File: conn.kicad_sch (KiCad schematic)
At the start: 74 parts, among them J10 MicroFit_2x04, J11 JST_S4B-XH, J12 MicroFit_2x04, J13 JST_B2B-XH, J14 JST_S2B-XH, J15 DNI, J16 MLX_1x03, J17 MLX_1x03, J5 JST_S6B-XH, J6 JST_S4B-XH, J7 MicroFit_2x04, J8 JST_S4B-XH, J9 JST_S4B-XH, SW2 DNI

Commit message: Mostly groundplane declutter and loop removal.
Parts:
- renumbered D23 to D22, D22 to D23, NT26 to NT25, NT27 to NT26, NT25 to NT27, RN8 to RN7, RN7 to RN8
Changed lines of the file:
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@@
   (symbol (lib_id "power:GND") (at 147.32 58.42 0) (unit 1)
     (in_bom yes) (on_board yes)
-    (property "Reference" "#PWR046" (id 0) (at 147.32 64.77 0)
+    (property "Reference" "#PWR049" (id 0) (at 147.32 64.77 0)
       (effects (font (size 1.27 1.27)) hide)
     )
@@
   (symbol (lib_id "power:GND") (at 67.31 118.11 0) (unit 1)
     (in_bom yes) (on_board yes)
-    (property "Reference" "#PWR041" (id 0) (at 67.31 124.46 0)
+    (property "Reference" "#PWR042" (id 0) (at 67.31 124.46 0)
       (effects (font (size 1.27 1.27)) hide)
     )
@@
   (symbol (lib_id "3rd-party:NT_2_TT") (at 154.94 109.22 0) (unit 1)
     (in_bom yes) (on_board yes)
-    (property "Reference" "NT26" (id 0) (at 154.94 108.62 0)
+    (property "Reference" "NT25" (id 0) (at 154.94 108.62 0)
       (effects (font (size 0.6 0.6)))
     )
@@
   (symbol (lib_id "3rd-party:NT_2_TT") (at 167.64 80.01 90) (unit 1)
     (in_bom yes) (on_board yes)
-    (property "Reference" "NT25" (id 0) (at 167.04 80.01 0)
+    (property "Reference" "NT27" (id 0) (at 167.04 80.01 0)
       (effects (font (size 0.6 0.6)))
     )
@@
   (symbol (lib_id "power:GND") (at 87.63 58.42 0) (unit 1)
     (in_bom yes) (on_board yes)
-    (property "Reference" "#PWR042" (id 0) (at 87.63 64.77 0)
+    (property "Reference" "#PWR044" (id 0) (at 87.63 64.77 0)
       (effects (font (size 1.27 1.27)) hide)
     )
@@
   (symbol (lib_id "power:GND") (at 267.97 158.75 0) (unit 1)
     (in_bom yes) (on_board yes)
-    (property "Reference" "#PWR037" (id 0) (at 267.97 165.1 0)
+    (property "Reference" "#PWR058" (id 0) (at 267.97 165.1 0)
       (effects (font (size 1.27 1.27)) hide)
     )
@@
   (symbol (lib_id "power:+5V") (at 60.96 151.13 0) (unit 1)
     (in_bom yes) (on_board yes)
-    (property "Reference" "#PWR039" (id 0) (at 60.96 154.94 0)
+    (property "Reference" "#PWR040" (id 0) (at 60.96 154.94 0)
       (effects (font (size 1.27 1.27)) hide)
     )
@@
   (symbol (lib_id "Device:LED") (at 259.08 83.82 0) (unit 1)
     (in_bom yes) (on_board yes)
-    (property "Reference" "D22" (id 0) (at 255.27 80.01 0))
+    (property "Reference" "D23" (id 0) (at 255.27 80.01 0))
     (property "Value" "GRN" (id 1) (at 262.89 82.55 0))
     (property "Footprint" "-Project:LED_0402_DOT" (id 2) (at 259.08 83.82 0)
@@
   (symbol (lib_id "Device:R_Pack04") (at 236.22 85.09 270) (mirror x) (unit 1)
     (in_bom yes) (on_board yes)
-    (property "Reference" "RN8" (id 0) (at 233.68 93.98 90)
+    (property "Reference" "RN7" (id 0) (at 233.68 93.98 90)
       (effects (font (size 1.27 1.27)) (justify left))
     )
@@
   (symbol (lib_id "power:GND") (at 81.28 83.82 0) (unit 1)
     (in_bom yes) (on_board yes)
-    (property "Reference" "#PWR0103" (id 0) (at 81.28 90.17 0)
+    (property "Reference" "#PWR043" (id 0) (at 81.28 90.17 0)
       (effects (font (size 1.27 1.27)) hide)
     )
@@
   (symbol (lib_id "power:GND") (at 116.84 58.42 0) (unit 1)
     (in_bom yes) (on_board yes)
-    (property "Reference" "#PWR044" (id 0) (at 116.84 64.77 0)
+    (property "Reference" "#PWR047" (id 0) (at 116.84 64.77 0)
       (effects (font (size 1.27 1.27)) hide)
     )
@@
   (symbol (lib_id "power:GND") (at 187.96 73.66 0) (unit 1)
     (in_bom yes) (on_board yes)
-    (property "Reference" "#PWR051" (id 0) (at 187.96 80.01 0)
+    (property "Reference" "#PWR055" (id 0) (at 187.96 80.01 0)
       (effects (font (size 1.27 1.27)) hide)
     )
@@
   (symbol (lib_id "Device:R_Pack04") (at 236.22 134.62 270) (mirror x) (unit 1)
     (in_bom yes) (on_board yes)
-    (property "Reference" "RN7" (id 0) (at 233.68 143.51 90)
+    (property "Reference" "RN8" (id 0) (at 233.68 143.51 90)
       (effects (font (size 1.27 1.27)) (justify left))
     )
@@
   (symbol (lib_id "power:GND") (at 110.49 83.82 0) (unit 1)
     (in_bom yes) (on_board yes)
-    (property "Reference" "#PWR0102" (id 0) (at 110.49 90.17 0)
+    (property "Reference" "#PWR045" (id 0) (at 110.49 90.17 0)
       (effects (font (size 1.27 1.27)) hide)
     )
@@
   (symbol (lib_id "Device:LED") (at 259.08 78.74 180) (unit 1)
     (in_bom yes) (on_board yes)
-    (property "Reference" "D23" (id 0) (at 255.27 82.55 0))
+    (property "Reference" "D22" (id 0) (at 255.27 82.55 0))
     (property "Value" "RED" (id 1) (at 262.89 80.01 0))
     (property "Footprint" "-Project:LED_0402_DOT" (id 2) (at 259.08 78.74 0)
@@
   (symbol (lib_id "power:GND") (at 60.96 178.435 0) (unit 1)
     (in_bom yes) (on_board yes)
-    (property "Reference" "#PWR040" (id 0) (at 60.96 184.785 0)
+    (property "Reference" "#PWR041" (id 0) (at 60.96 184.785 0)
       (effects (font (size 1.27 1.27)) hide)
     )
@@
   (symbol (lib_id "power:+5V") (at 116.84 33.02 0) (unit 1)
     (in_bom yes) (on_board yes)
-    (property "Reference" "#PWR043" (id 0) (at 116.84 36.83 0)
+    (property "Reference" "#PWR046" (id 0) (at 116.84 36.83 0)
       (effects (font (size 1.27 1.27)) hide)
     )
@@
   (symbol (lib_id "power:GND") (at 165.1 130.175 0) (unit 1)
     (in_bom yes) (on_board yes)
-    (property "Reference" "#PWR047" (id 0) (at 165.1 136.525 0)
+    (property "Reference" "#PWR050" (id 0) (at 165.1 136.525 0)
       (effects (font (size 1.27 1.27)) hide)
     )
@@
   (symbol (lib_id "power:GND") (at 267.97 54.61 0) (unit 1)
     (in_bom yes) (on_board yes)
-    (property "Reference" "#PWR0105" (id 0) (at 267.97 60.96 0)
+    (property "Reference" "#PWR056" (id 0) (at 267.97 60.96 0)
       (effects (font (size 1.27 1.27)) hide)
     )
@@
   (symbol (lib_id "3rd-party:NT_2_TT") (at 154.94 111.76 0) (unit 1)
     (in_bom yes) (on_board yes)
-    (property "Reference" "NT27" (id 0) (at 154.94 111.16 0)
+    (property "Reference" "NT26" (id 0) (at 154.94 111.16 0)
       (effects (font (size 0.6 0.6)))
     )
@@
   (symbol (lib_id "power:GND") (at 267.97 106.68 0) (unit 1)
     (in_bom yes) (on_board yes)
-    (property "Reference" "#PWR053" (id 0) (at 267.97 113.03 0)
+    (property "Reference" "#PWR057" (id 0) (at 267.97 113.03 0)
       (effects (font (size 1.27 1.27)) hide)
     )
@@
   (symbol (lib_id "power:+5V") (at 167.64 77.47 0) (unit 1)
     (in_bom yes) (on_board yes)
-    (property "Reference" "#PWR045" (id 0) (at 167.64 81.28 0)
+    (property "Reference" "#PWR051" (id 0) (at 167.64 81.28 0)
       (effects (font (size 1.27 1.27)) hide)
     )
@@
   (symbol (lib_id "power:GND") (at 187.96 49.53 0) (unit 1)
     (in_bom yes) (on_board yes)
-    (property "Reference" "#PWR050" (id 0) (at 187.96 55.88 0)
+    (property "Reference" "#PWR054" (id 0) (at 187.96 55.88 0)
       (effects (font (size 1.27 1.27)) hide)
     )
@@
   (symbol (lib_id "power:GND") (at 140.97 85.09 0) (unit 1)
     (in_bom yes) (on_board yes)
-    (property "Reference" "#PWR0104" (id 0) (at 140.97 91.44 0)
+    (property "Reference" "#PWR048" (id 0) (at 140.97 91.44 0)
       (effects (font (size 1.27 1.27)) hide)
     )
@@
   (symbol (lib_id "power:+5V") (at 179.07 39.37 0) (unit 1)
     (in_bom yes) (on_board yes)
-    (property "Reference" "#PWR048" (id 0) (at 179.07 43.18 0)
+    (property "Reference" "#PWR052" (id 0) (at 179.07 43.18 0)
       (effects (font (size 1.27 1.27)) hide)
     )
@@
   (symbol (lib_id "power:+5V") (at 179.07 63.5 0) (unit 1)
     (in_bom yes) (on_board yes)
-    (property "Reference" "#PWR049" (id 0) (at 179.07 67.31 0)
-      (effects (font (size 1.27 1.27)) hide)
-    )
+    (property "Reference" "#PWR053" (id 0) (at 179.07 67.31 0)
+      (effects (font (size 1.27 1.27)) hide)
+    )

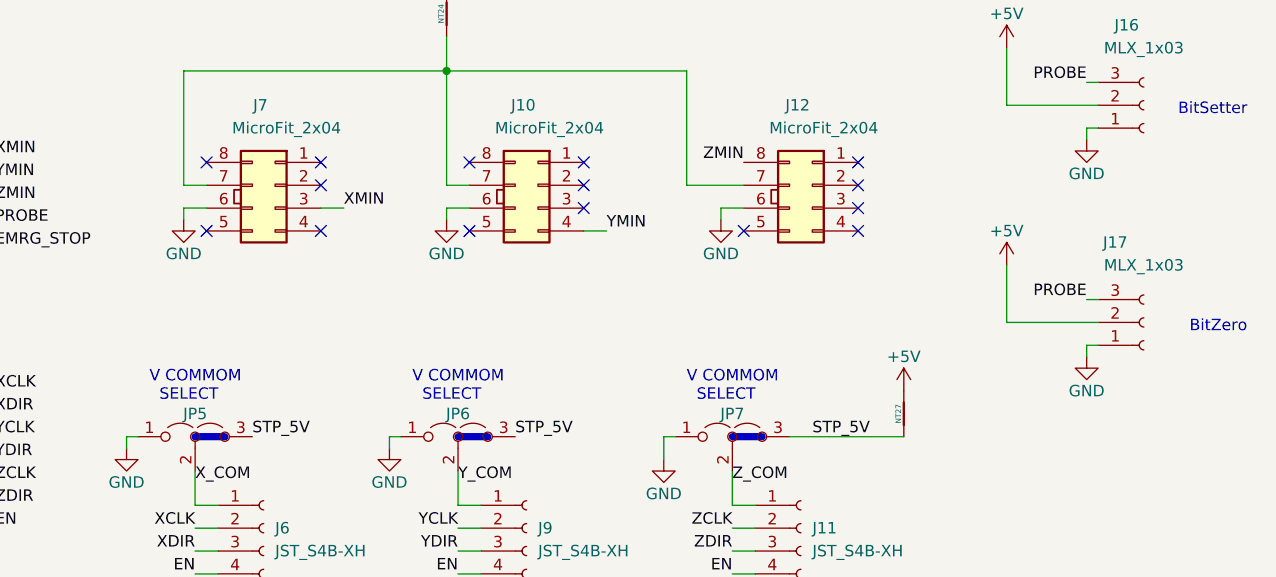
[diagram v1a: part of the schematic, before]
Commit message: Fixed opto-isolator wrong part and added jumper to isolate A/DGNDs.
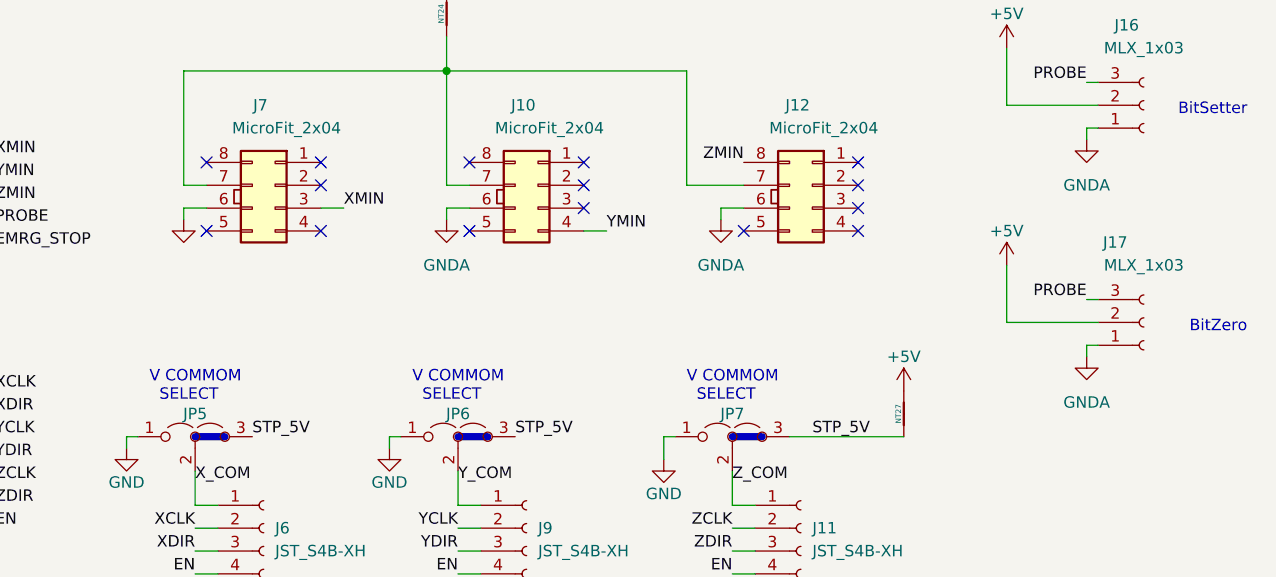
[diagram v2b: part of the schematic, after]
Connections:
- net GND: no longer J10.6 (Pin_6), J12.6 (Pin_6), J16.1 (Pin_1), J17.1 (Pin_1), J7.6 (Pin_6)
- new net GNDA: J10.6 (Pin_6), J12.6 (Pin_6), J16.1 (Pin_1), J17.1 (Pin_1), J7.6 (Pin_6)
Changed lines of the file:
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@@
     (pin "3")
-  )
-  (symbol (lib_id "power:GND") (at 147.32 58.42 0) (unit 1)
-    (in_bom yes) (on_board yes)
-    (property "Reference" "#PWR049" (id 0) (at 147.32 64.77 0)
-      (effects (font (size 1.27 1.27)) hide)
-    )
-    (property "Value" "GND" (id 1) (at 147.32 62.23 0))
-    (property "Footprint" "" (id 2) (at 147.32 58.42 0)
-      (effects (font (size 1.27 1.27)) hide)
-    )
-    (property "Datasheet" "" (id 3) (at 147.32 58.42 0)
-      (effects (font (size 1.27 1.27)) hide)
-    )
-    (pin "1")
   )
   (symbol (lib_id "Device:LED") (at 259.08 22.86 0) (unit 1)
@@
     (pin "2")
   )
+  (symbol (lib_id "power:GNDA") (at 147.32 58.42 0) (unit 1)
+    (in_bom yes) (on_board yes) (fields_autoplaced)
+    (property "Reference" "#PWR063" (id 0) (at 147.32 64.77 0)
+      (effects (font (size 1.27 1.27)) hide)
+    )
+    (property "Value" "GNDA" (id 1) (at 147.32 63.5 0))
+    (property "Footprint" "" (id 2) (at 147.32 58.42 0)
+      (effects (font (size 1.27 1.27)) hide)
+    )
+    (property "Datasheet" "" (id 3) (at 147.32 58.42 0)
+      (effects (font (size 1.27 1.27)) hide)
+    )
+    (pin "1")
+  )
   (symbol (lib_id "3rd-party:NT_2_TT") (at 50.8 170.18 0) (unit 1)
     (in_bom yes) (on_board yes)
@@
     (pin "1")
     (pin "2")
-  )
-  (symbol (lib_id "power:GND") (at 87.63 58.42 0) (unit 1)
-    (in_bom yes) (on_board yes)
-    (property "Reference" "#PWR044" (id 0) (at 87.63 64.77 0)
-      (effects (font (size 1.27 1.27)) hide)
-    )
-    (property "Value" "GND" (id 1) (at 87.63 62.23 0))
-    (property "Footprint" "" (id 2) (at 87.63 58.42 0)
-      (effects (font (size 1.27 1.27)) hide)
-    )
-    (property "Datasheet" "" (id 3) (at 87.63 58.42 0)
-      (effects (font (size 1.27 1.27)) hide)
-    )
-    (pin "1")
   )
   (symbol (lib_id "Device:LED") (at 119.38 160.02 0) (unit 1)
@@
     (pin "8")
   )
+  (symbol (lib_id "power:GNDA") (at 87.63 58.42 0) (unit 1)
+    (in_bom yes) (on_board yes) (fields_autoplaced)
+    (property "Reference" "#PWR055" (id 0) (at 87.63 64.77 0)
+      (effects (font (size 1.27 1.27)) hide)
+    )
+    (property "Value" "" (id 1) (at 87.63 63.5 0))
+    (property "Footprint" "" (id 2) (at 87.63 58.42 0)
+      (effects (font (size 1.27 1.27)) hide)
+    )
+    (property "Datasheet" "" (id 3) (at 87.63 58.42 0)
+      (effects (font (size 1.27 1.27)) hide)
+    )
+    (pin "1")
+  )
   (symbol (lib_id "Connector:Conn_01x03_Female") (at 194.31 69.85 0) (mirror x) (unit 1)
     (in_bom yes) (on_board yes)
@@
     (pin "2")
     (pin "3")
+  )
+  (symbol (lib_id "power:GNDA") (at 187.96 49.53 0) (unit 1)
+    (in_bom yes) (on_board yes) (fields_autoplaced)
+    (property "Reference" "#PWR064" (id 0) (at 187.96 55.88 0)
+      (effects (font (size 1.27 1.27)) hide)
+    )
+    (property "Value" "GNDA" (id 1) (at 187.96 54.61 0))
+    (property "Footprint" "" (id 2) (at 187.96 49.53 0)
+      (effects (font (size 1.27 1.27)) hide)
+    )
+    (property "Datasheet" "" (id 3) (at 187.96 49.53 0)
+      (effects (font (size 1.27 1.27)) hide)
+    )
+    (pin "1")
   )
   (symbol (lib_id "Device:LED") (at 119.38 165.1 0) (unit 1)
@@
     (pin "2")
   )
+  (symbol (lib_id "power:GNDA") (at 187.96 73.66 0) (unit 1)
+    (in_bom yes) (on_board yes) (fields_autoplaced)
+    (property "Reference" "#PWR065" (id 0) (at 187.96 80.01 0)
+      (effects (font (size 1.27 1.27)) hide)
+    )
+    (property "Value" "GNDA" (id 1) (at 187.96 78.74 0))
+    (property "Footprint" "" (id 2) (at 187.96 73.66 0)
+      (effects (font (size 1.27 1.27)) hide)
+    )
+    (property "Datasheet" "" (id 3) (at 187.96 73.66 0)
+      (effects (font (size 1.27 1.27)) hide)
+    )
+    (pin "1")
+  )
   (symbol (lib_id "power:GND") (at 81.28 83.82 0) (unit 1)
     (in_bom yes) (on_board yes)
@@
     (pin "1")
     (pin "2")
-  )
-  (symbol (lib_id "power:GND") (at 116.84 58.42 0) (unit 1)
-    (in_bom yes) (on_board yes)
-    (property "Reference" "#PWR047" (id 0) (at 116.84 64.77 0)
-      (effects (font (size 1.27 1.27)) hide)
-    )
-    (property "Value" "GND" (id 1) (at 116.84 62.23 0))
-    (property "Footprint" "" (id 2) (at 116.84 58.42 0)
-      (effects (font (size 1.27 1.27)) hide)
-    )
-    (property "Datasheet" "" (id 3) (at 116.84 58.42 0)
-      (effects (font (size 1.27 1.27)) hide)
-    )
-    (pin "1")
   )
   (symbol (lib_id "Device:LED") (at 259.08 148.59 180) (unit 1)
@@
     (pin "2")
   )
-  (symbol (lib_id "power:GND") (at 187.96 73.66 0) (unit 1)
-    (in_bom yes) (on_board yes)
-    (property "Reference" "#PWR055" (id 0) (at 187.96 80.01 0)
-      (effects (font (size 1.27 1.27)) hide)
-    )
-    (property "Value" "GND" (id 1) (at 187.96 77.47 0))
-    (property "Footprint" "" (id 2) (at 187.96 73.66 0)
-      (effects (font (size 1.27 1.27)) hide)
-    )
-    (property "Datasheet" "" (id 3) (at 187.96 73.66 0)
-      (effects (font (size 1.27 1.27)) hide)
-    )
-    (pin "1")
-  )
   (symbol (lib_id "Connector:Conn_01x04_Female") (at 96.52 92.71 0) (unit 1)
     (in_bom yes) (on_board yes)
@@
     (pin "2")
   )
+  (symbol (lib_id "power:GNDA") (at 116.84 58.42 0) (unit 1)
+    (in_bom yes) (on_board yes) (fields_autoplaced)
+    (property "Reference" "#PWR062" (id 0) (at 116.84 64.77 0)
+      (effects (font (size 1.27 1.27)) hide)
+    )
+    (property "Value" "GNDA" (id 1) (at 116.84 63.5 0))
+    (property "Footprint" "" (id 2) (at 116.84 58.42 0)
+      (effects (font (size 1.27 1.27)) hide)
+    )
+    (property "Datasheet" "" (id 3) (at 116.84 58.42 0)
+      (effects (font (size 1.27 1.27)) hide)
+    )
+    (pin "1")
+  )
   (symbol (lib_id "Connector:Conn_01x06_Female") (at 71.12 170.18 0) (mirror x) (unit 1)
     (in_bom yes) (on_board yes)
@@
     (pin "2")
   )
-  (symbol (lib_id "power:GND") (at 187.96 49.53 0) (unit 1)
-    (in_bom yes) (on_board yes)
-    (property "Reference" "#PWR054" (id 0) (at 187.96 55.88 0)
-      (effects (font (size 1.27 1.27)) hide)
-    )
-    (property "Value" "GND" (id 1) (at 187.96 53.34 0))
-    (property "Footprint" "" (id 2) (at 187.96 49.53 0)
-      (effects (font (size 1.27 1.27)) hide)
-    )
-    (property "Datasheet" "" (id 3) (at 187.96 49.53 0)
-      (effects (font (size 1.27 1.27)) hide)
-    )
-    (pin "1")
-  )
   (symbol (lib_id "power:GND") (at 140.97 85.09 0) (unit 1)

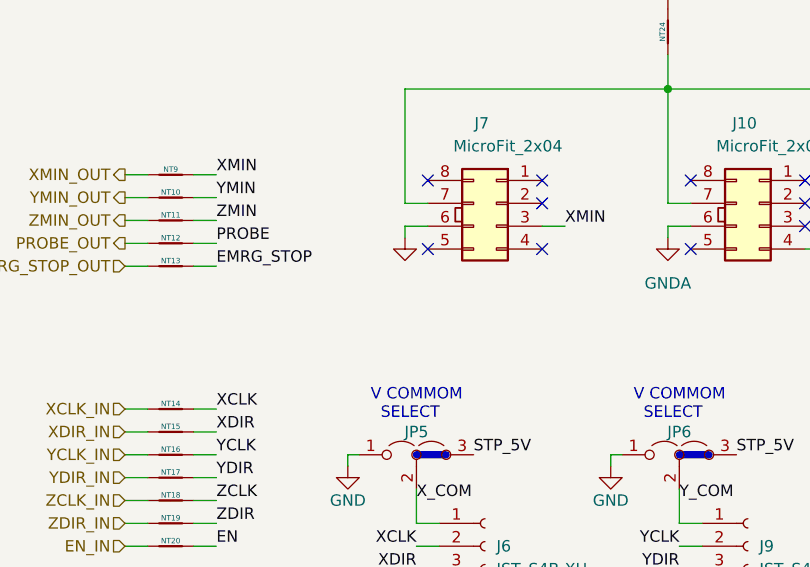
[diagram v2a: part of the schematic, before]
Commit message: Chnaged opto-couplers to 3-ch versions. Cheaper and less waste[.|?]
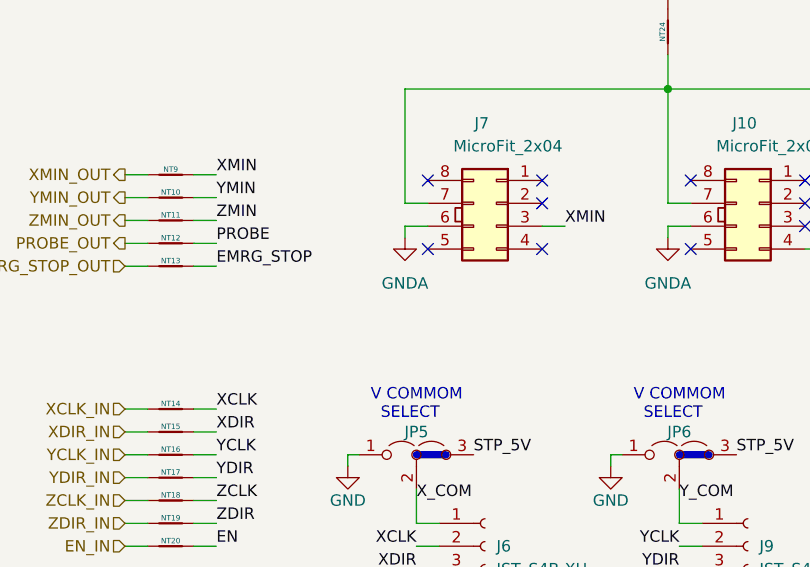
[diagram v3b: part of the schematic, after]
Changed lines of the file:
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@@
       (effects (font (size 1.27 1.27)) hide)
     )
-    (property "Value" "" (id 1) (at 87.63 63.5 0))
+    (property "Value" "GNDA" (id 1) (at 87.63 63.5 0))
     (property "Footprint" "" (id 2) (at 87.63 58.42 0)
       (effects (font (size 1.27 1.27)) hide)
